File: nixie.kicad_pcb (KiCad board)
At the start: 4 copper layers, 189 x 55 mm, 70 parts, among them J1 Barrel_Jack, J2 Conn_01x02_Pin, Q1 2N3906, Q2 IRF644, SW1 RotaryEncoder_Switch, U1 4504, U2 MC34063AP, U3 HV5222PG-G, U4 LM7805_TO220, U5 HV5222PG-G, U6 ATmega328P-P, U7 DS3231MZ

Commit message: automatic date/version control
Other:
- board text added: "Nixie Clock by Pim Borman Version ${VERSION} Date ${DATE} https://github.com/pimborman/nixie-clock"
- board text removed: "Nixie Clock | Pim Borman version 1.0 https://github.com/pimborman/nixie-clock"
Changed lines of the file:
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@@
 	(title_block
 		(title "Nixie Clock Project")
-		(date "2024-10-03")
-		(rev "1.0")
+		(date "${DATE}")
+		(rev "${VERSION}")
 		(company "Pim Borman")
 	)
@@
 		(tags "Integrated Circuit")
 		(property "Reference" "SW1"
-			(at -9.5 -14.9 360)
+			(at -9.5 -14.9 0)
 			(layer "F.SilkS")
 			(effects
@@
 		(layer "Edge.Cuts")
 	)
-	(gr_text "Nixie Clock | Pim Borman\nversion 1.0\nhttps://github.com/pimborman/nixie-clock\n\n"
+	(gr_text "Nixie Clock by Pim Borman\nVersion ${VERSION}\nDate ${DATE}\nhttps://github.com/pimborman/nixie-clock\n\n"
 		(at 252 69.2 0)
 		(layer "B.SilkS")

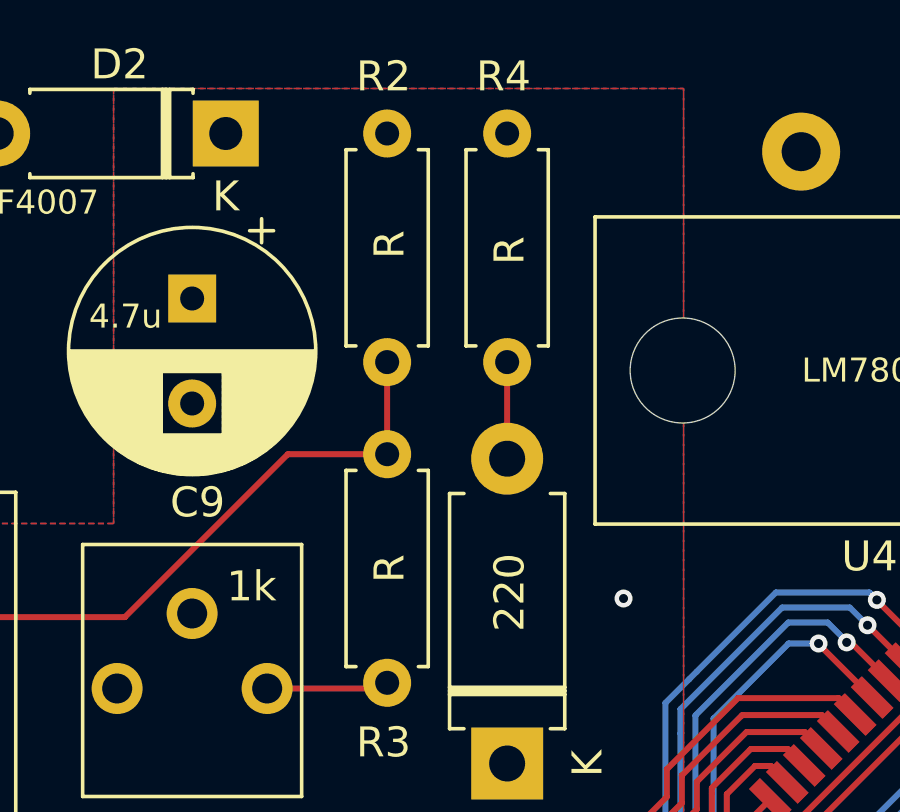
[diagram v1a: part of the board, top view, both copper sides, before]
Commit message: added 3D model, added missing component values, improved interactive bom
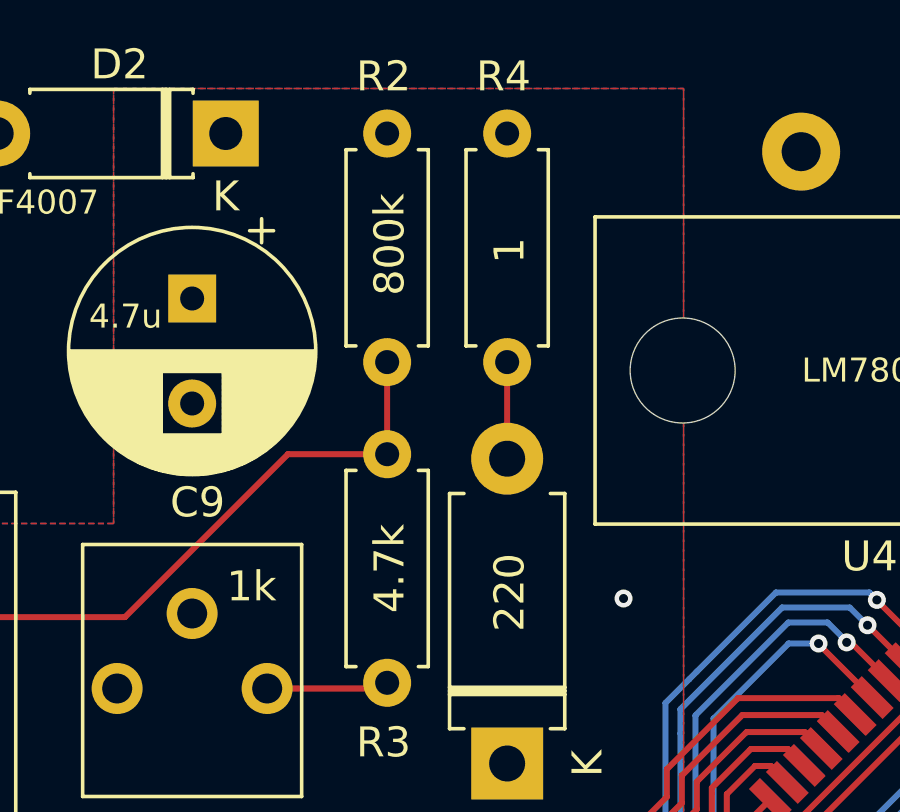
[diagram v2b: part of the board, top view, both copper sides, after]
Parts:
- R2: value R -> 800k
- R3: value R -> 4.7k
- R4: value R -> 1
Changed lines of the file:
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@@
 		)
 	)
+	(property "DATE" "2024-10-13")
+	(property "VERSION" "v1.0")
 	(net 0 "")
 	(net 1 "GND")
@@
 		(at 108.12 85 90)
 		(descr "Potentiometer, vertical, Bourns 3386P, https://www.bourns.com/pdfs/3386.pdf")
-		(tags "Potentiometer vertical Bourns 3386P")
+		(tags "Potentiometer vertical Bourns 3306P")
 		(property "Reference" "RV1"
 			(at -4.8 -2.32 180)
@@
 			(layer "F.Fab")
 		)
+		(fp_text user "${REFERENCE}"
+			(at -4.95 -3.05 180)
+			(layer "F.Fab")
+			(effects
+				(font
+					(size 1 1)
+					(thickness 0.15)
+				)
+			)
+		)
 		(pad "1" thru_hole circle
 			(at 0 0 90)
@@
 			(pintype "passive")
 		)
-		(model "${KIPRJMOD}/packages3D/Potentiometer_Bourns_3386P_Vertical.wrl"
+		(model "${KIPRJMOD}/packages3D/3306P-1-103.STEP"
 			(offset
-				(xyz 0 0 0)
+				(xyz 1.25 2.5 0)
 			)
 			(scale
@@
 			)
 			(rotate
-				(xyz 0 0 0)
+				(xyz -90 0 90)
 			)
 		)
@@
 			)
 		)
-		(property "Value" "R"
+		(property "Value" "1"
 			(at 3.9 -0.08 90)
 			(layer "F.SilkS")
@@
 			)
 		)
-		(property "Value" "R"
+		(property "Value" "800k"
 			(at 3.92 0.08 90)
 			(layer "F.SilkS")
@@
 			)
 		)
-		(property "Value" "R"
+		(property "Value" "4.7k"
 			(at 3.81 0.08 90)
 			(layer "F.SilkS")
